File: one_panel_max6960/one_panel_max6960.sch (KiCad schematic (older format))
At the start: 13 parts, among them M1 LED-MATRIX-8X8, P1 CONN_12, P2 CONN_12, P3 CONN_2, U1 MAX6960

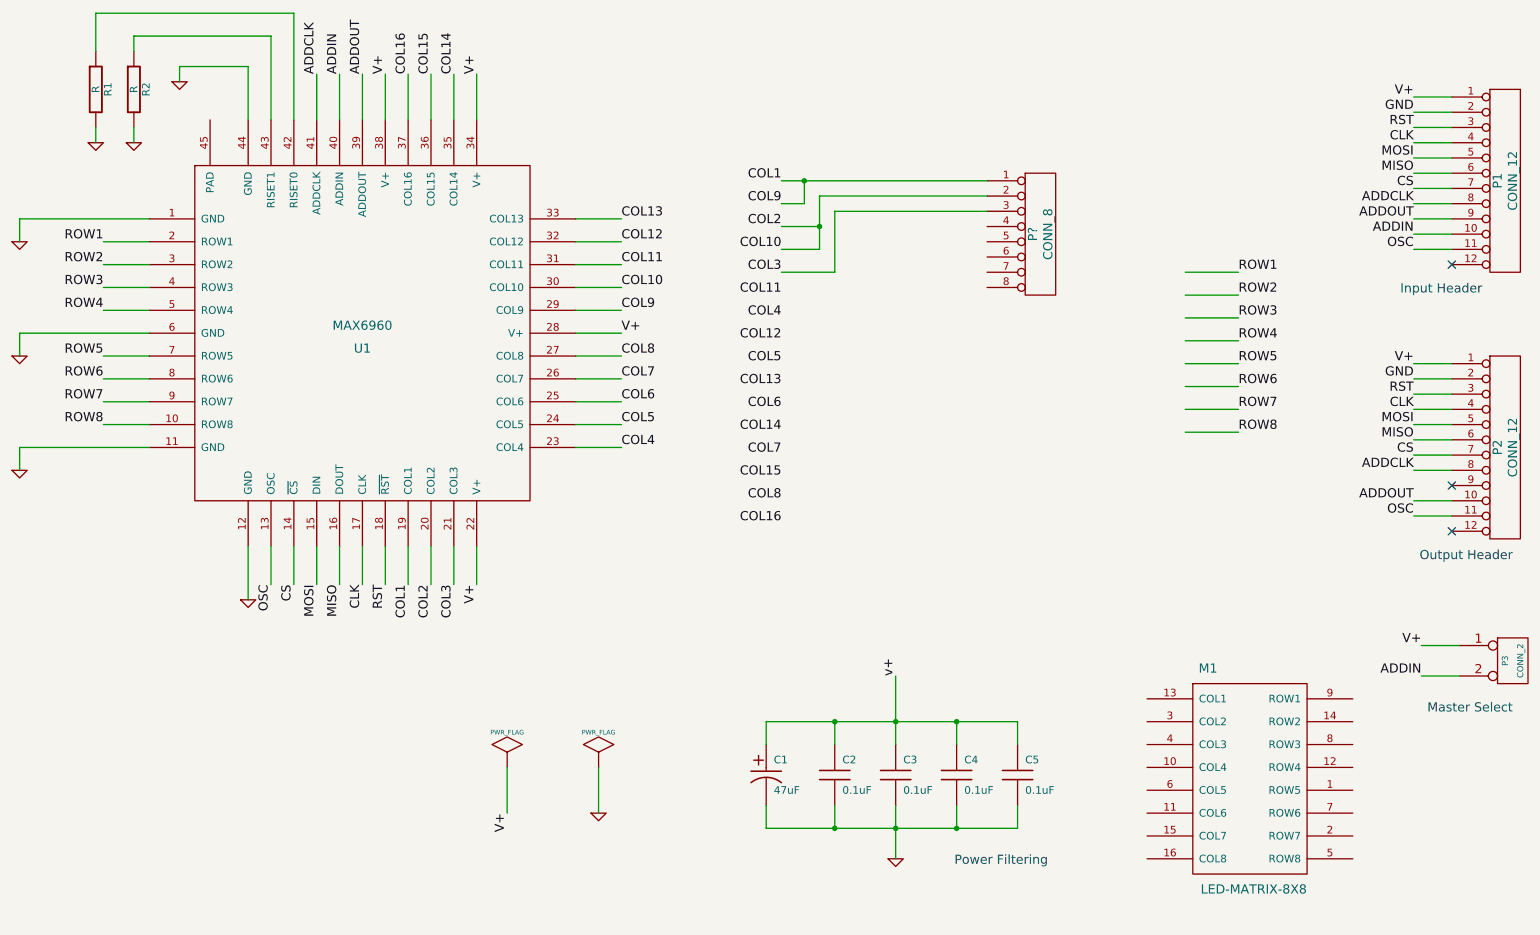
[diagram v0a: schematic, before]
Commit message: Added new one panel version of the max6960 design.
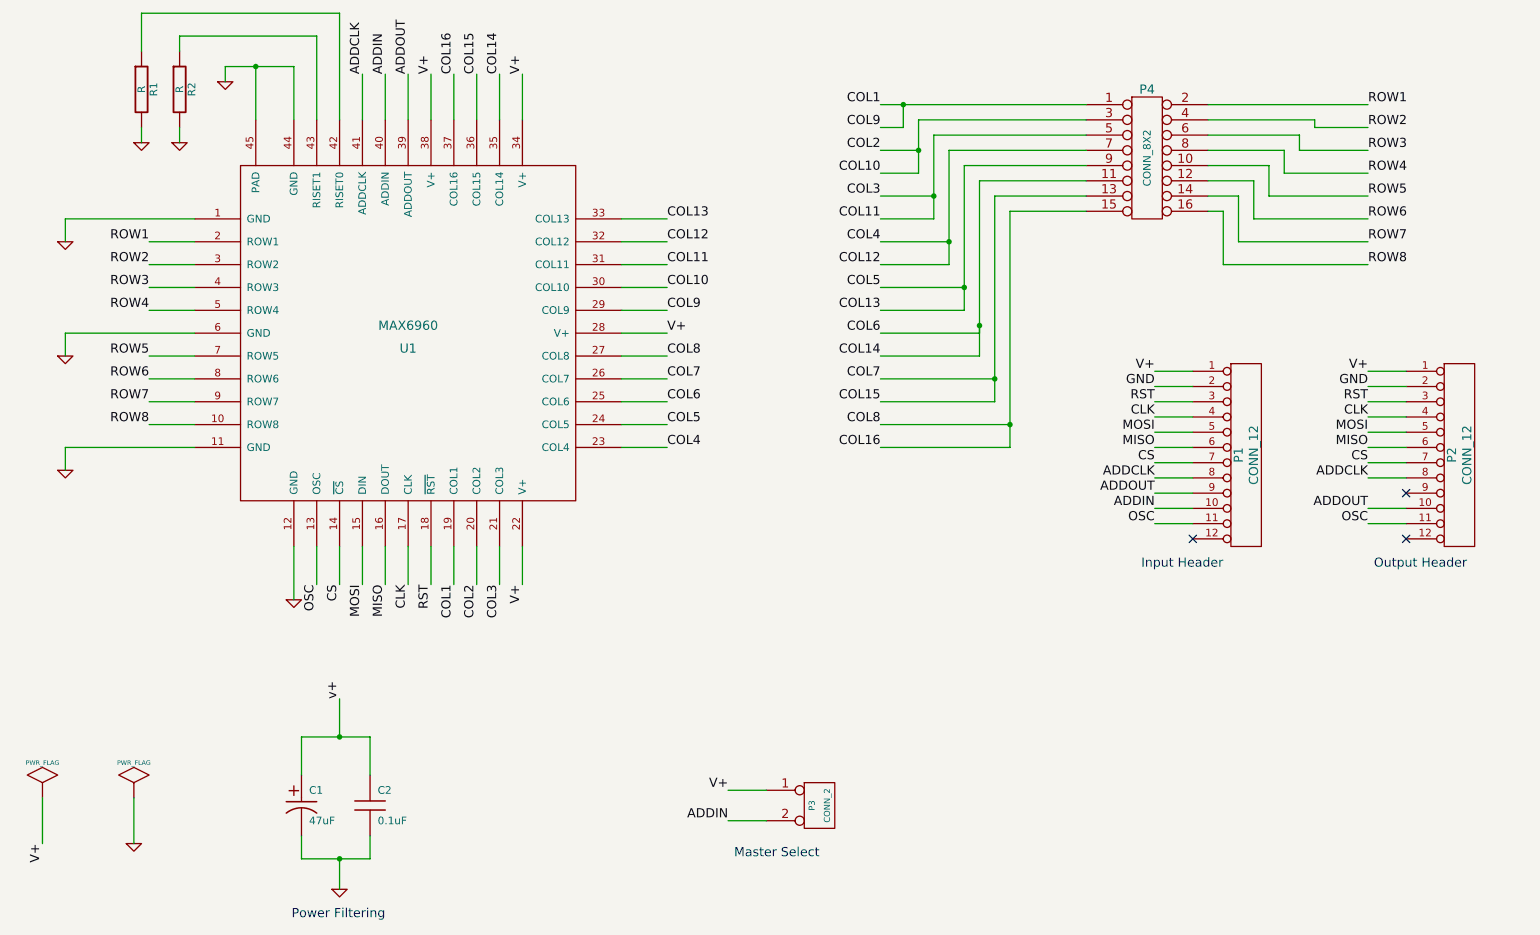
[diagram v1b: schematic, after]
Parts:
- removed C3, C4, C5: 0.1uF, symbol C
- removed M1: LED-MATRIX-8X8, symbol LED-MATRIX-8X8
- removed P?: CONN_8, symbol CONN_8
- added P4: CONN_8X2, symbol CONN_8X2
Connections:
- wire segments 110 -> 143
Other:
- moved on the sheet: C1, C2, P1, P2, P3, R1, R2, U1
